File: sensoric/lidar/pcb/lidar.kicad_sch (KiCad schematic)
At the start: 13 parts, among them J1 TWI, J2 TFMini-Plus, J3 28BYJ-48, SW1 SW_Push, U1 ATmega8L-8PU, U2 ULN2003A, Y1 16 MHz

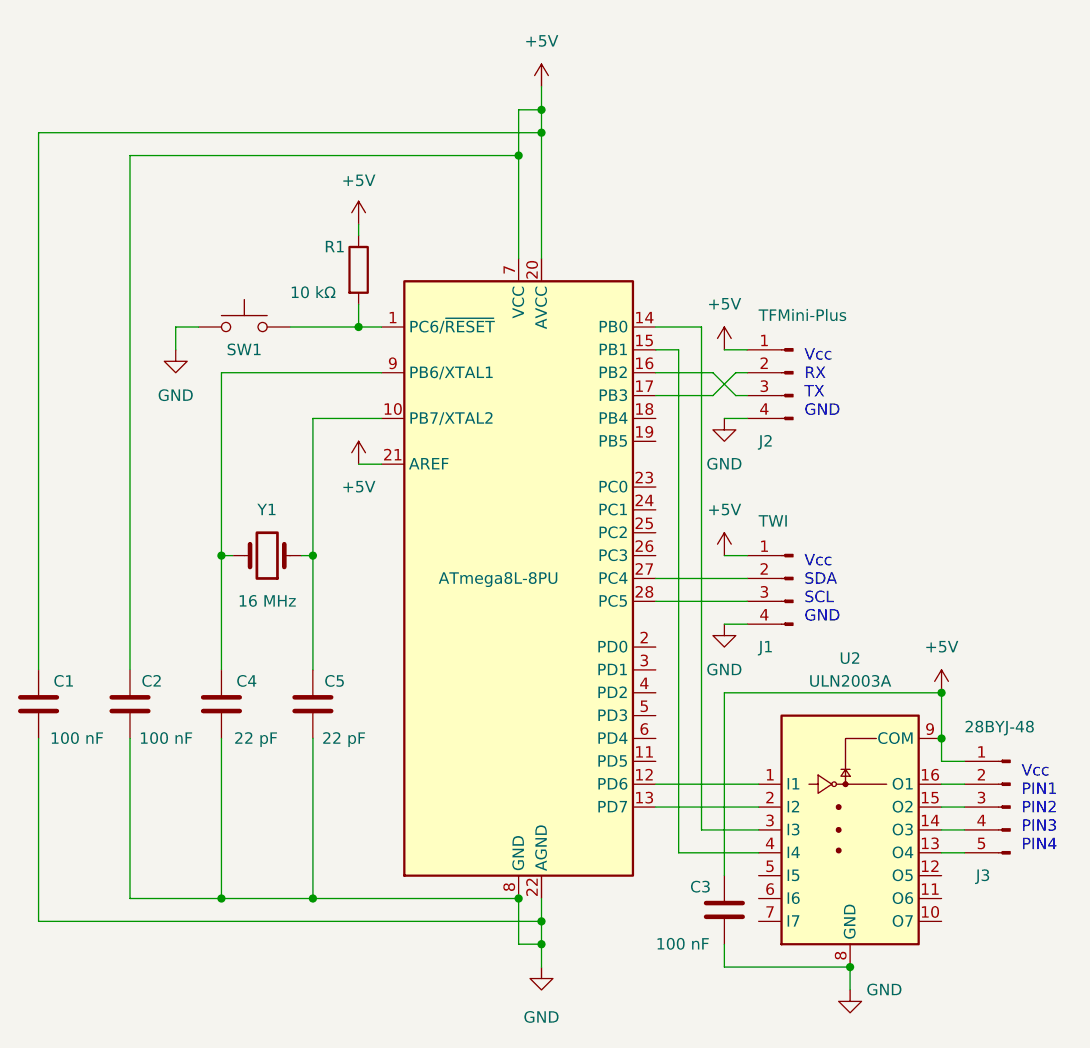
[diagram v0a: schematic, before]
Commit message: refactor: moved from stepper motor to servo
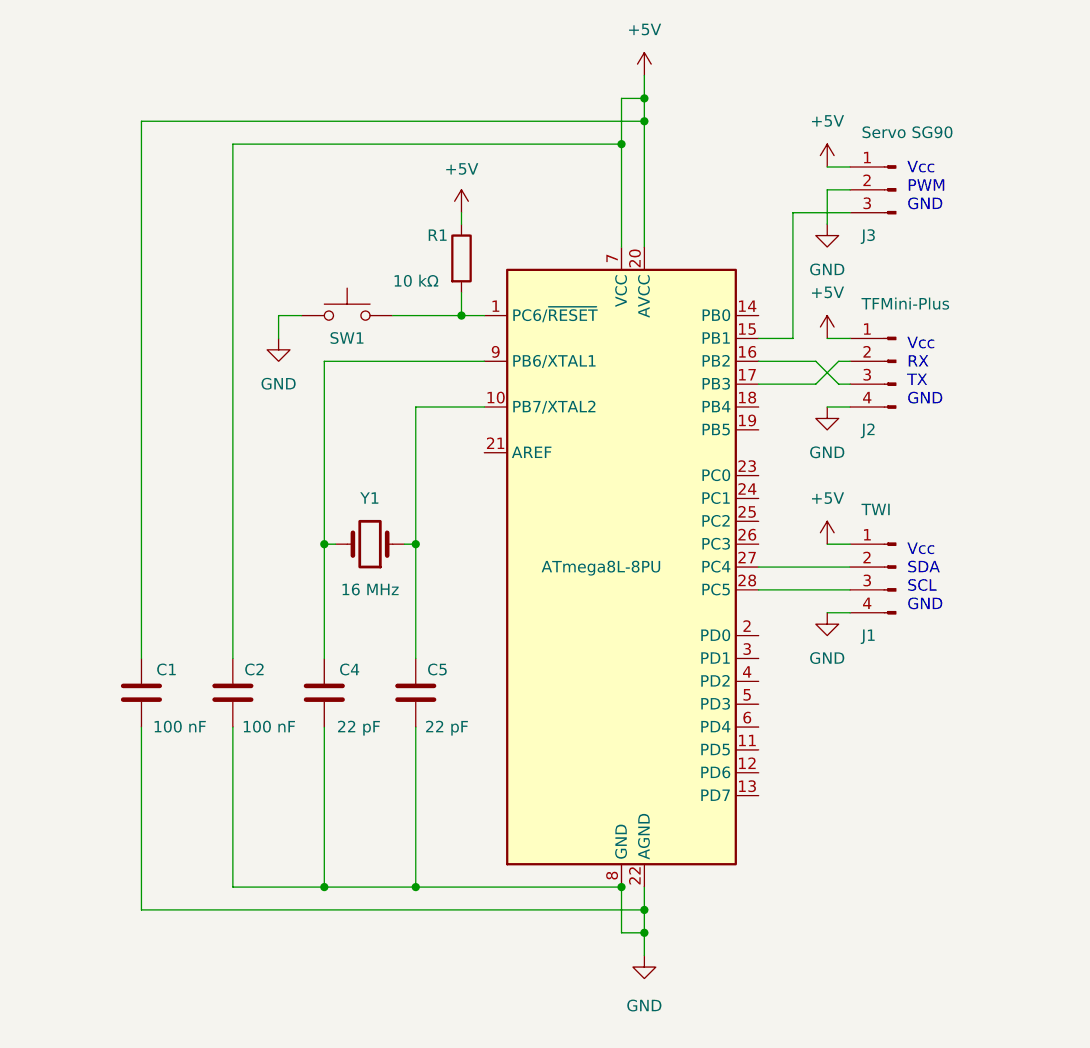
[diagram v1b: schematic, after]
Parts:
- removed C3: 100 nF, Capacitor_THT:C_Disc_D4.3mm_W1.9mm_P5.00mm, symbol Device:C
- removed J3: 28BYJ-48, Connector_PinHeader_2.54mm:PinHeader_1x05_P2.54mm_Vertical, symbol Connector:Conn_01x05_Male
- removed U2: ULN2003A, Package_DIP:DIP-16_W7.62mm_Socket, symbol Transistor_Array:ULN2003A
- added J3: Servo SG90, Connector_PinHeader_2.54mm:PinHeader_1x03_P2.54mm_Vertical, symbol Connector:Conn_01x03_Male
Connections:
- net +5V: now also J3.1 (Pin_1); no longer U1.21 (AREF)
- net GND: now also J3.2 (Pin_2)
- net at U1.15 (PB1): now also J3.3 (Pin_3)
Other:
- note added: "Vcc PWM GND"
- note removed: "Vcc PIN1 PIN2 PIN3 PIN4"
- moved on the sheet: C1, C2, C4, C5, J1, J2, R1, SW1, Y1
